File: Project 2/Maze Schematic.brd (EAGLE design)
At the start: 152.4 x 165.1 mm, 33 parts, among them SW1 BUTTON, SW2 BUTTON, SW3 BUTTON, SW4 BUTTON, SW5 BUTTON, U1 MOD-LED8X8RGB-CONN, U2 MPU-9250, U3 POCKETBEAGLE, U6 MOD-LED8X8RGB-CONN

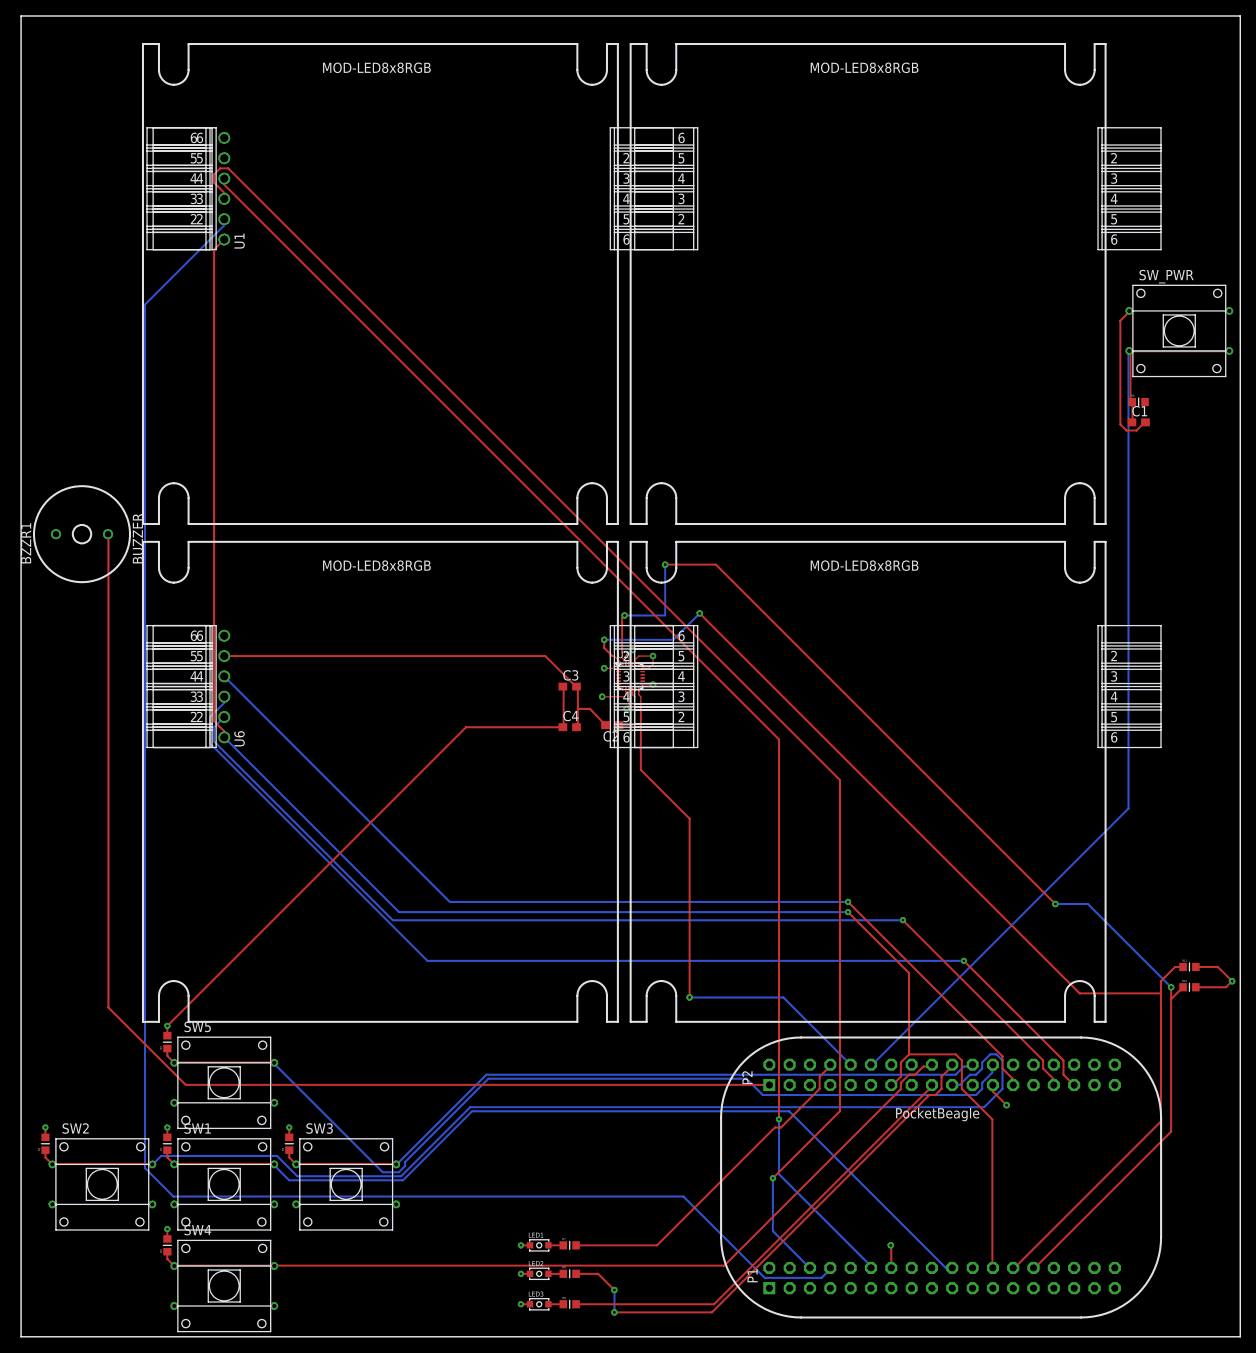
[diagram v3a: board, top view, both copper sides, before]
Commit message: Added Documentation and mounting holes, as well as a pdf version of board and schematic
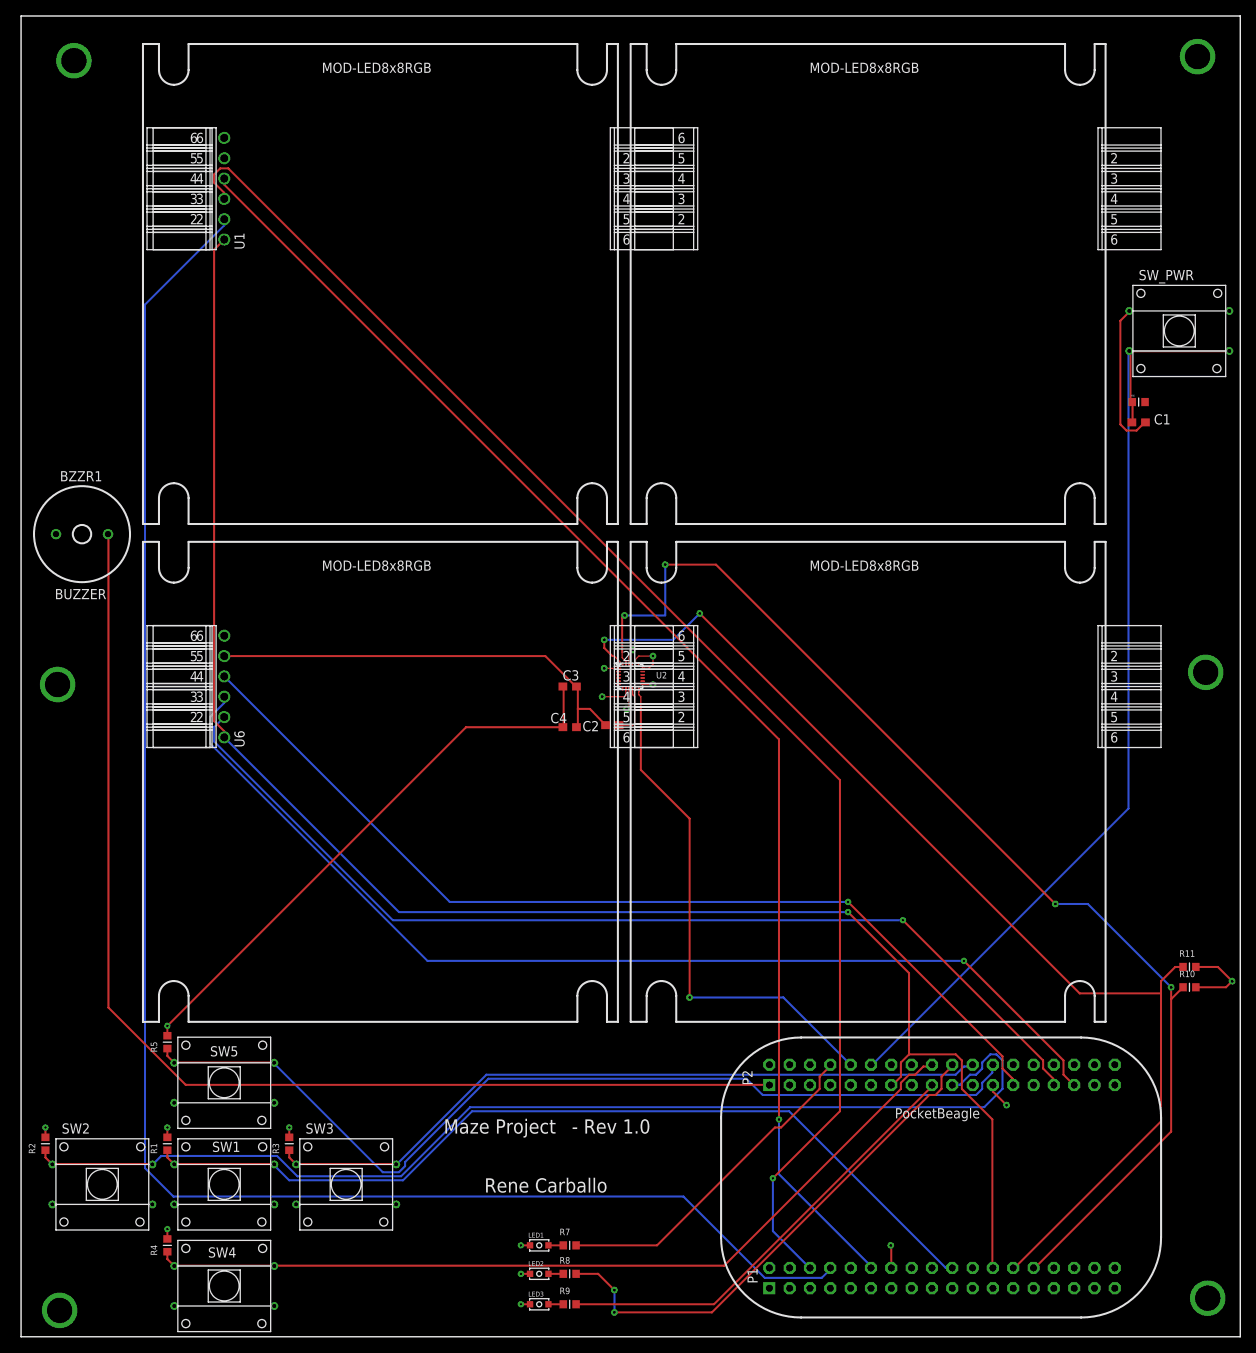
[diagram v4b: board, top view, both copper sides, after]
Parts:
- added MGT1, MGT2, MGT3, MGT4, MGT5, MGT6: MOUNTING_HOLE, Buzzer Box:MOUNTING_HOLE
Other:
- board text added: "- Rev 1.0"
- board text added: "Maze Project"
- board text added: "Rene Carballo"
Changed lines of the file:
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@@
 <?xml version="1.0" encoding="utf-8"?>
 <!DOCTYPE eagle SYSTEM "eagle.dtd">
-<eagle version="8.7.1">
+<eagle version="9.0.0">
 <drawing>
 <settings>
@@
 <layer number="27" name="tValues" color="7" fill="1" visible="yes" active="yes"/>
 <layer number="28" name="bValues" color="7" fill="1" visible="yes" active="yes"/>
-<layer number="29" name="tStop" color="7" fill="3" visible="no" active="yes"/>
-<layer number="30" name="bStop" color="7" fill="6" visible="no" active="yes"/>
-<layer number="31" name="tCream" color="7" fill="4" visible="no" active="yes"/>
-<layer number="32" name="bCream" color="7" fill="5" visible="no" active="yes"/>
-<layer number="33" name="tFinish" color="6" fill="3" visible="no" active="yes"/>
-<layer number="34" name="bFinish" color="6" fill="6" visible="no" active="yes"/>
-<layer number="35" name="tGlue" color="7" fill="4" visible="no" active="yes"/>
-<layer number="36" name="bGlue" color="7" fill="5" visible="no" active="yes"/>
-<layer number="37" name="tTest" color="7" fill="1" visible="no" active="yes"/>
-<layer number="38" name="bTest" color="7" fill="1" visible="no" active="yes"/>
+<layer number="29" name="tStop" color="7" fill="3" visible="yes" active="yes"/>
+<layer number="30" name="bStop" color="7" fill="6" visible="yes" active="yes"/>
+<layer number="31" name="tCream" color="7" fill="4" visible="yes" active="yes"/>
+<layer number="32" name="bCream" color="7" fill="5" visible="yes" active="yes"/>
+<layer number="33" name="tFinish" color="6" fill="3" visible="yes" active="yes"/>
+<layer number="34" name="bFinish" color="6" fill="6" visible="yes" active="yes"/>
+<layer number="35" name="tGlue" color="7" fill="4" visible="yes" active="yes"/>
+<layer number="36" name="bGlue" color="7" fill="5" visible="yes" active="yes"/>
+<layer number="37" name="tTest" color="7" fill="1" visible="yes" active="yes"/>
+<layer number="38" name="bTest" color="7" fill="1" visible="yes" active="yes"/>
 <layer number="39" name="tKeepout" color="4" fill="11" visible="yes" active="yes"/>
 <layer number="40" name="bKeepout" color="1" fill="11" visible="yes" active="yes"/>
@@
 <layer number="42" name="bRestrict" color="1" fill="10" visible="yes" active="yes"/>
 <layer number="43" name="vRestrict" color="2" fill="10" visible="yes" active="yes"/>
-<layer number="44" name="Drills" color="7" fill="1" visible="no" active="yes"/>
-<layer number="45" name="Holes" color="7" fill="1" visible="no" active="yes"/>
-<layer number="46" name="Milling" color="3" fill="1" visible="no" active="yes"/>
-<layer number="47" name="Measures" color="7" fill="1" visible="no" active="yes"/>
+<layer number="44" name="Drills" color="7" fill="1" visible="yes" active="yes"/>
+<layer number="45" name="Holes" color="7" fill="1" visible="yes" active="yes"/>
+<layer number="46" name="Milling" color="3" fill="1" visible="yes" active="yes"/>
+<layer number="47" name="Measures" color="7" fill="1" visible="yes" active="yes"/>
 <layer number="48" name="Document" color="7" fill="1" visible="yes" active="yes"/>
 <layer number="49" name="Reference" color="7" fill="1" visible="yes" active="yes"/>
@@
 <wire x1="152.4" y1="165.1" x2="0" y2="165.1" width="0" layer="20"/>
 <wire x1="0" y1="165.1" x2="0" y2="0" width="0" layer="20"/>
+<text x="52.832" y="25.4" size="1.778" layer="25">Maze Project</text>
+<text x="57.912" y="18.034" size="1.778" layer="25">Rene Carballo</text>
+<text x="68.834" y="25.4" size="1.778" layer="25">- Rev 1.0</text>
 </plain>
 <attributes>
@@
 </autorouter>
 <elements>
-<element name="BZZR1" library="Buzzer Box" package="BUZZER-12MM" value="BUZZER" x="7.62" y="100.33" rot="R90"/>
+<element name="BZZR1" library="Buzzer Box" package="BUZZER-12MM" value="BUZZER" x="7.62" y="100.33" smashed="yes" rot="R90">
+<attribute name="NAME" x="10.16" y="108.204" size="1.27" layer="25" rot="R180"/>
+<attribute name="VALUE" x="10.668" y="93.472" size="1.27" layer="25" rot="R180"/>
+</element>
 <element name="LED3" library="Buzzer Box" package="LED-SMD" value="LTST-C191TBKT" x="64.77" y="4.064"/>
 <element name="U1" library="Buzzer Box" package="FE06W" value="MOD-LED8X8RGB-CONN" x="25.4" y="143.51" rot="R90"/>
-<element name="U2" library="Buzzer Box" package="QFN-3X3MM" value="MPU-9250" x="76.2" y="82.55"/>
+<element name="U2" library="Buzzer Box" package="QFN-3X3MM" value="MPU-9250" x="76.2" y="82.55" smashed="yes">
+<attribute name="NAME" x="79.375" y="82.296" size="0.8128" layer="25"/>
+<attribute name="VALUE" x="67.437" y="84.328" size="0.8128" layer="27"/>
+</element>
 <element name="U3" library="Buzzer Box" package="POCKETBEAGLE" value="POCKETBEAGLE" x="87.63" y="2.54"/>
 <element name="LED2" library="Buzzer Box" package="LED-SMD" value="LTST-C191TBKT" x="64.77" y="7.874"/>
@@
 <element name="SW_PWR" library="Buzzer Box" package="BUTTON-11.5X11.7MM" value="BUTTON" x="144.78" y="125.73"/>
 <element name="U6" library="Buzzer Box" package="FE06W" value="MOD-LED8X8RGB-CONN" x="25.4" y="81.28" rot="R90"/>
-<element name="SW1" library="Buzzer Box" package="BUTTON-11.5X11.7MM" value="BUTTON" x="25.4" y="19.05"/>
+<element name="SW1" library="Buzzer Box" package="BUTTON-11.5X11.7MM" value="BUTTON" x="25.4" y="19.05" smashed="yes">
+<attribute name="NAME" x="23.876" y="23.114" size="1.27" layer="25"/>
+<attribute name="VALUE" x="22.352" y="14.224" size="1.27" layer="27"/>
+</element>
 <element name="R1" library="Buzzer Box" package="R0603" value="1K" x="18.288" y="24.13" rot="R90"/>
 <element name="SW2" library="Buzzer Box" package="BUTTON-11.5X11.7MM" value="BUTTON" x="10.16" y="19.05"/>
@@
 <element name="SW3" library="Buzzer Box" package="BUTTON-11.5X11.7MM" value="BUTTON" x="40.64" y="19.05"/>
 <element name="R3" library="Buzzer Box" package="R0603" value="1K" x="33.528" y="24.13" rot="R90"/>
-<element name="SW4" library="Buzzer Box" package="BUTTON-11.5X11.7MM" value="BUTTON" x="25.4" y="6.35"/>
+<element name="SW4" library="Buzzer Box" package="BUTTON-11.5X11.7MM" value="BUTTON" x="25.4" y="6.35" smashed="yes">
+<attribute name="NAME" x="23.368" y="9.906" size="1.27" layer="25"/>
+<attribute name="VALUE" x="22.352" y="1.524" size="1.27" layer="27"/>
+</element>
 <element name="R4" library="Buzzer Box" package="R0603" value="1K" x="18.288" y="11.43" rot="R90"/>
-<element name="SW5" library="Buzzer Box" package="BUTTON-11.5X11.7MM" value="BUTTON" x="25.4" y="31.75"/>
+<element name="SW5" library="Buzzer Box" package="BUTTON-11.5X11.7MM" value="BUTTON" x="25.4" y="31.75" smashed="yes">
+<attribute name="NAME" x="23.622" y="35.052" size="1.27" layer="25"/>
+<attribute name="VALUE" x="22.352" y="26.924" size="1.27" layer="27"/>
+</element>
 <element name="R5" library="Buzzer Box" package="R0603" value="1K" x="18.288" y="36.83" rot="R90"/>
 <element name="U$1" library="Buzzer Box" package="MOD-LED8X8RGB" value="" x="76.2" y="101.6"/>
@@
 <element name="U$5" library="Buzzer Box" package="MOD-LED8X8RGB" value="" x="15.24" y="39.37"/>
 <element name="U$6" library="Buzzer Box" package="MOD-LED8X8RGB" value="" x="76.2" y="39.37"/>
-<element name="R6" library="Buzzer Box" package="R0603" value="10K" x="139.7" y="116.84"/>
-<element name="C1" library="Buzzer Box" package="C0603" value=".1uF" x="139.7" y="114.3"/>
+<element name="R6" library="Buzzer Box" package="R0603" value="10K" x="139.7" y="116.84" smashed="yes">
+<attribute name="NAME" x="138.7856" y="117.5004" size="0.254" layer="25"/>
+<attribute name="VALUE" x="138.5824" y="115.9002" size="0.254" layer="27"/>
+</element>
+<element name="C1" library="Buzzer Box" package="C0603" value=".1uF" x="139.7" y="114.3" smashed="yes">
+<attribute name="NAME" x="141.605" y="114.046" size="1.27" layer="25"/>
+<attribute name="VALUE" x="137.795" y="112.268" size="1.27" layer="27"/>
+</element>
 <element name="R7" library="Buzzer Box" package="R0603" value="1K" x="68.58" y="11.43"/>
 <element name="R8" library="Buzzer Box" package="R0603" value="1K" x="68.58" y="7.874"/>
 <element name="R9" library="Buzzer Box" package="R0603" value="1K" x="68.58" y="4.064"/>
-<element name="C2" library="Buzzer Box" package="C0603" value=".1uF" x="73.914" y="76.454" rot="R180"/>
+<element name="C2" library="Buzzer Box" package="C0603" value=".1uF" x="73.914" y="76.454" smashed="yes" rot="R180">
+<attribute name="NAME" x="72.263" y="76.962" size="1.27" layer="25" rot="R180"/>
+<attribute name="VALUE" x="73.787" y="75.438" size="1.27" layer="27" rot="R180"/>
+</element>
 <element name="C3" library="Buzzer Box" package="C0603" value=".1uF" x="68.58" y="81.28"/>
-<element name="C4" library="Buzzer Box" package="C0603" value="10nF" x="68.58" y="76.2"/>
+<element name="C4" library="Buzzer Box" package="C0603" value="10nF" x="68.58" y="76.2" smashed="yes">
+<attribute name="NAME" x="66.167" y="76.708" size="1.27" layer="25"/>
+<attribute name="VALUE" x="66.167" y="74.168" size="1.27" layer="27"/>
+</element>
 <element name="R10" library="Buzzer Box" package="R0603" value="1K" x="146.05" y="43.688"/>
 <element name="R11" library="Buzzer Box" package="R0603" value="1K" x="146.05" y="46.228"/>
+<element name="MGT1" library="Buzzer Box" package="MOUNTING_HOLE" value="MOUNTING_HOLE" x="6.604" y="159.512"/>
+<element name="MGT2" library="Buzzer Box" package="MOUNTING_HOLE" value="MOUNTING_HOLE" x="147.066" y="160.02"/>
+<element name="MGT3" library="Buzzer Box" package="MOUNTING_HOLE" value="MOUNTING_HOLE" x="4.572" y="81.534"/>
+<element name="MGT4" library="Buzzer Box" package="MOUNTING_HOLE" value="MOUNTING_HOLE" x="148.082" y="83.058"/>
+<element name="MGT5" library="Buzzer Box" package="MOUNTING_HOLE" value="MOUNTING_HOLE" x="148.336" y="4.826"/>
+<element name="MGT6" library="Buzzer Box" package="MOUNTING_HOLE" value="MOUNTING_HOLE" x="4.826" y="3.302"/>
 </elements>
 <signals>
